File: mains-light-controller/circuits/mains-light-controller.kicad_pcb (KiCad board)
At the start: 2 copper layers, 90.5 x 83 mm, 18 parts, among them J1 Screw_Terminal_01x03, J2 Screw_Terminal_01x02, Q1 BT136-500, U1 LTV-817, U2 HLK-PM05, U3 MOC3021M, U4 WeMos_mini

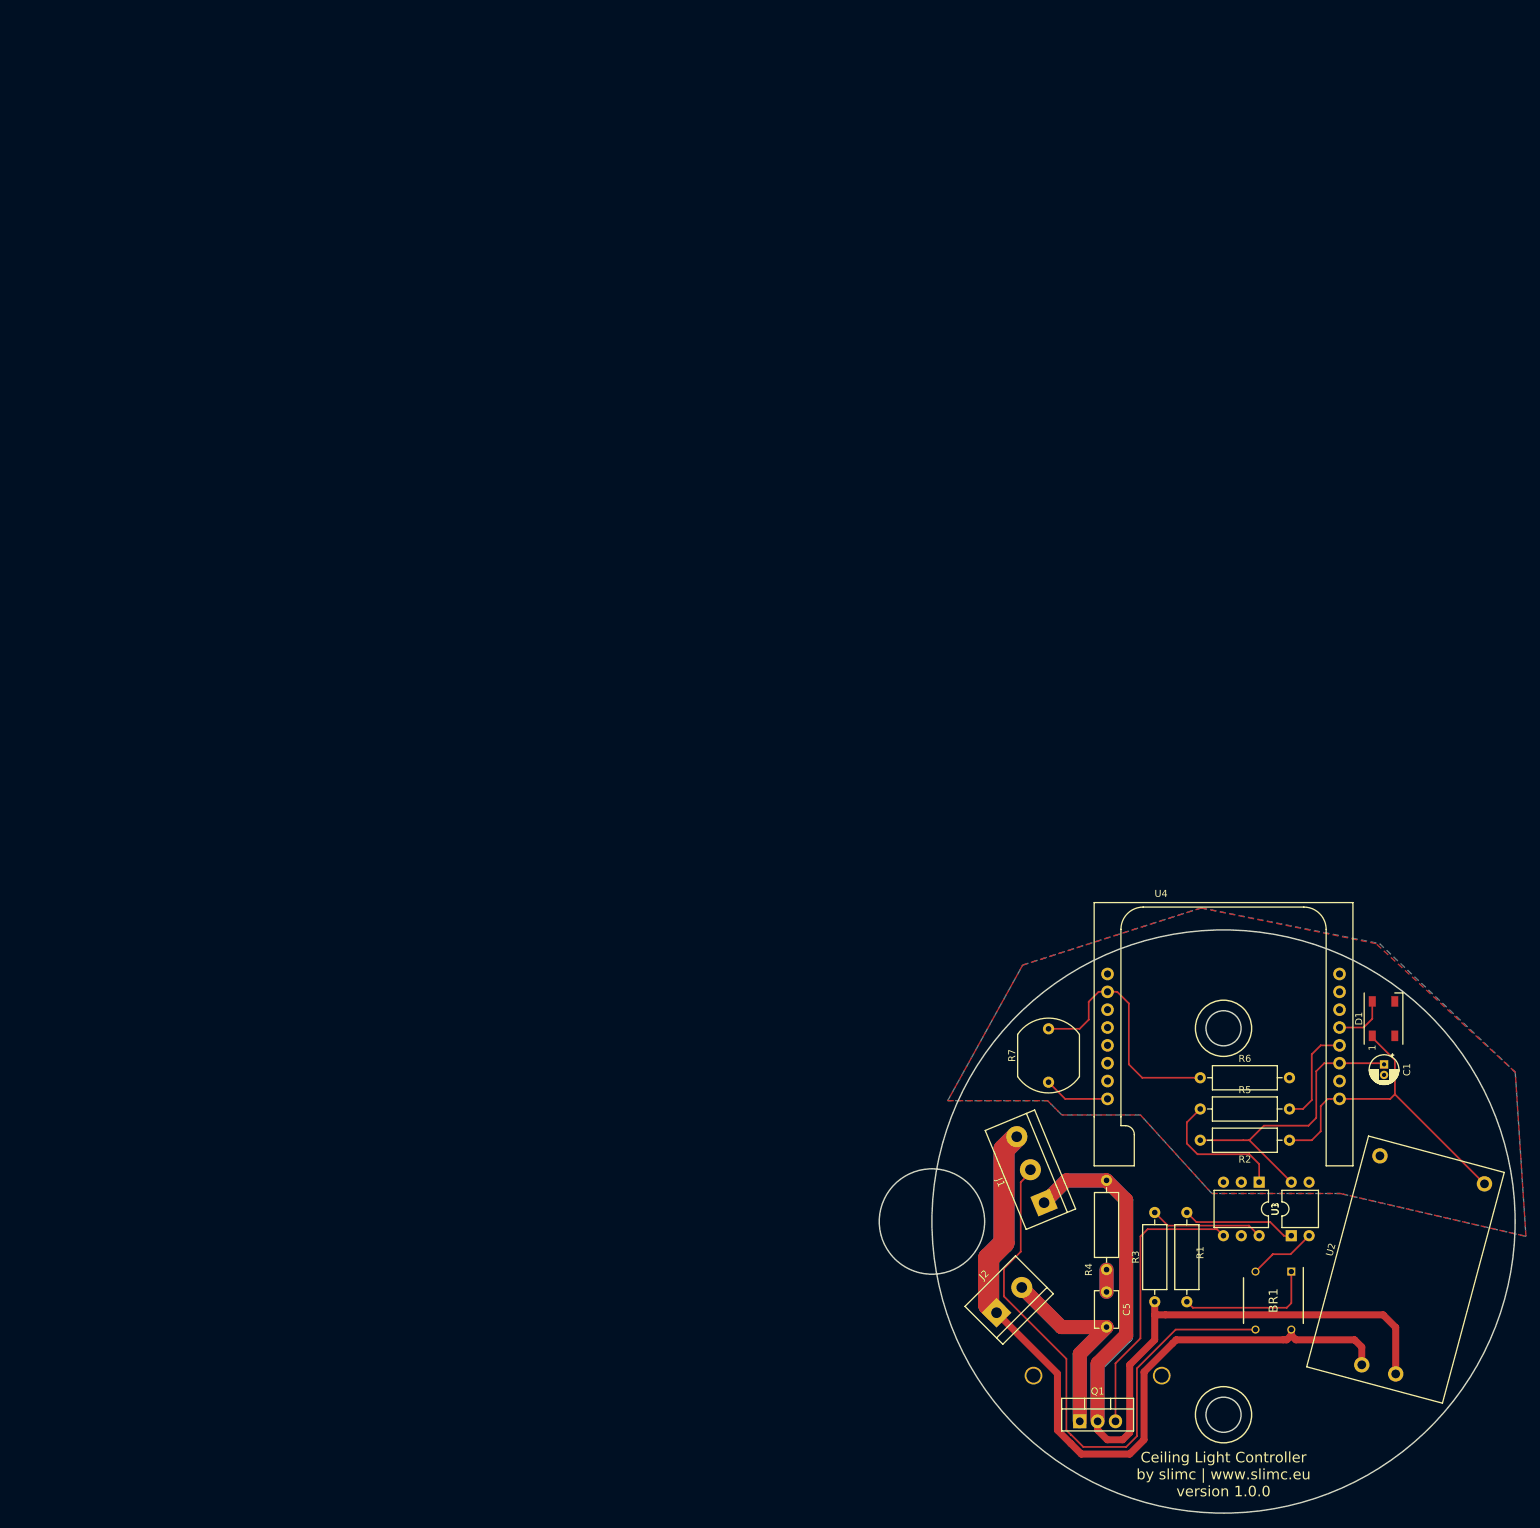
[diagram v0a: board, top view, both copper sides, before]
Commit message: improved schematic layout view; missing new PCB layout
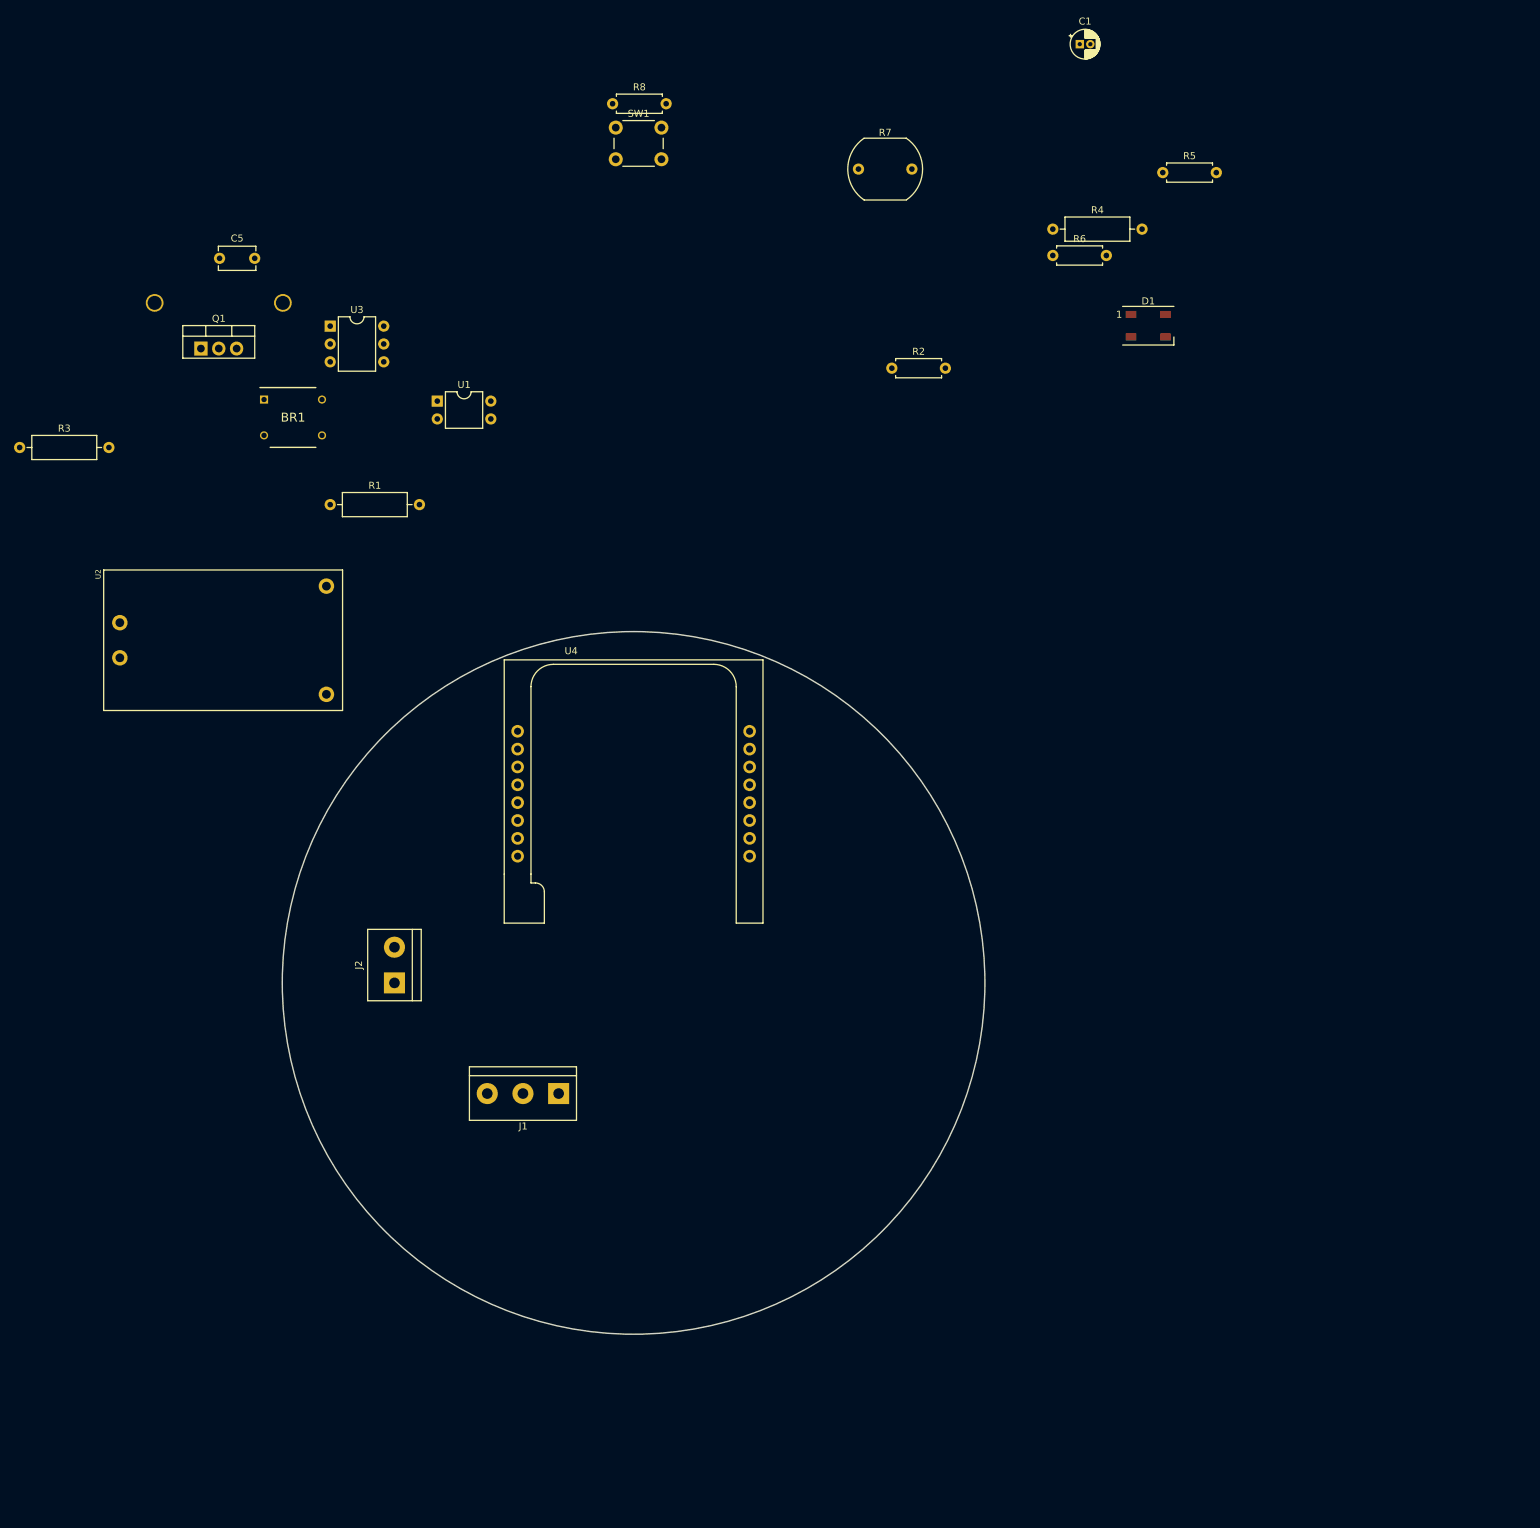
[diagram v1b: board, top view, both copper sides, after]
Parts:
- added R8: 10K, Resistor_THT:R_Axial_DIN0207_L6.3mm_D2.5mm_P7.62mm_Horizontal, F.Cu at (63.1, -59.1)
- added SW1: SW_Push, Button_Switch_THT:SW_PUSH_6mm, F.Cu at (63.5, -55.7)
- C1: value 1µf -> 1µF
- C5: value 100nf -> 100NF
- R1: value 390k -> 390K
- R2: value 10k -> 10K; footprint Resistor_THT:R_Axial_DIN0309_L9.0mm_D3.2mm_P12.70mm_Horizontal -> Resistor_THT:R_Axial_DIN0207_L6.3mm_D2.5mm_P7.62mm_Horizontal
- R3: value 10k -> 10K
- R4: value 100 -> 100R
- R5: value 330 -> 33R; footprint Resistor_THT:R_Axial_DIN0309_L9.0mm_D3.2mm_P12.70mm_Horizontal -> Resistor_THT:R_Axial_DIN0207_L6.3mm_D2.5mm_P7.62mm_Horizontal
- R6: value 10000 -> 10K; footprint Resistor_THT:R_Axial_DIN0309_L9.0mm_D3.2mm_P12.70mm_Horizontal -> Resistor_THT:R_Axial_DIN0207_L6.3mm_D2.5mm_P7.62mm_Horizontal
- U2: footprint Power_Supply:HLK-PM05 -> Power_Supply:HLK-PM01
- moved R3 202.2 mm to (-21.3, -10.2), turned to 0 degrees
- moved Q1 197.4 mm to (4.46, -24.2)
- moved C5 193.8 mm to (7.11, -37.1), turned to 0 degrees
- moved U2 190.6 mm to (7.62, 17.3), turned to 0 degrees
- moved BR1 187.8 mm to (17.6, -14.4), turned to 0 degrees
- moved U3 179.8 mm to (22.9, -27.4), turned to 0 degrees
- moved U1 169.9 mm to (38.1, -16.8), turned to 0 degrees
- moved R1 158.2 mm to (22.9, -2.03), turned to 0 degrees
- moved C1 151.5 mm to (129.5, -67.6), turned to 0 degrees
- moved R4 135.6 mm to (125.7, -41.2), turned to 0 degrees
- moved R5 133.4 mm to (141.4, -49.3)
- moved R7 132.7 mm to (98.0, -49.8), turned to 0 degrees
- moved R2 123.6 mm to (102.8, -21.4), turned to 0 degrees
- moved R6 118.9 mm to (125.7, -37.5)
- moved D1 104.1 mm to (139.3, -27.5), turned to 0 degrees
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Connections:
- net Net-(C5-Pad2) renamed L_OUT
- net Net-(R6-Pad1) renamed A0
- net Net-(U4-Pad12) renamed D5
- net Net-(U4-Pad13) renamed D6
- net Net-(U4-Pad14) renamed D7
- net Net-(U4-Pad7) renamed RX
- net Net-(U4-Pad8) renamed TX
- net Net-(U4-Pad9) renamed RST
- BR1 pad 3: Net-(BR1-Pad3) -> N_MAIN
- BR1 pad 4: Net-(BR1-Pad4) -> M1_IN
- C1 pad 1: Net-(C1-Pad1) -> D0
- D1 pad 1: Net-(D1-Pad1) -> +3V3
- D1 pad 4: Net-(D1-Pad4) -> D8
- J1 pad 1: Net-(J1-Pad1) -> N_MAIN
- J1 pad 2: Net-(BR1-Pad3) -> M2_IN
- J1 pad 3: Net-(BR1-Pad4) -> M1_IN
- J2 pad 1: Net-(BR1-Pad4) -> N_MAIN
- Q1 pad 2: Net-(J1-Pad1) -> M2_IN
- R2 pad 1: Net-(D1-Pad1) -> D0
- R2 pad 2: Net-(C1-Pad1) -> +5V
- R3 pad 1: Net-(J1-Pad1) -> M2_IN
- R4 pad 1: Net-(J1-Pad1) -> M2_IN
- R5 pad 2: Net-(R5-Pad2) -> D1
- R7 pad 1: Net-(R7-Pad1) -> +3V3
- U1 pad 4: Net-(C1-Pad1) -> D0
- U2 pad 1: Net-(BR1-Pad4) -> M2_IN
- U2 pad 2: Net-(J1-Pad1) -> N_MAIN
- U2 pad 4: Net-(D1-Pad1) -> +5V
- U4 pad 1: Net-(D1-Pad1) -> +5V
- U4 pad 11: Net-(U4-Pad11) -> D0
- U4 pad 15: Net-(U4-Pad15) -> D8
- U4 pad 16: Net-(R7-Pad1) -> +3V3
- U4 pad 3: Net-(C1-Pad1) -> D4
- U4 pad 4: Net-(R5-Pad2) -> D3
- U4 pad 5: Net-(D1-Pad4) -> D2
- U4 pad 6: Net-(U4-Pad6) -> D1
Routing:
- net Net-(J1-Pad1): track 163.5 -> 0.00 mm
- net Net-(BR1-Pad4): track 138.6 -> 0.00 mm
- net Net-(BR1-Pad3): track 82.6 -> 0.00 mm
- net L_OUT: track 58.8 -> 0.00 mm
- net Net-(D1-Pad1): track 47.5 -> 0.00 mm
- net Net-(C1-Pad1): track 43.1 -> 0.00 mm
- net Net-(Q1-Pad3): track 40.4 -> 0.00 mm
- net A0: track 35.4 -> 0.00 mm
- net Net-(BR1-Pad1): track 20.0 -> 0.00 mm
- net Net-(R5-Pad1): track 19.8 -> 0.00 mm
- net Net-(R3-Pad2): track 16.2 -> 0.00 mm
- net Net-(R1-Pad1): track 16.2 -> 0.00 mm
- net Net-(R5-Pad2): track 14.7 -> 0.00 mm
- net Net-(BR1-Pad2): track 9.77 -> 0.00 mm
- net Net-(R7-Pad1): track 9.38 -> 0.00 mm
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- removed copper zone on B.Cu, net GND
- removed copper zone on F.Cu, net GND
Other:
- board size 90.5 x 83 mm -> 100 x 100 mm
- board text removed: "Ceiling Light Controller by slimc | www.slimc.eu version 1.0.0"

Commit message: Schematic changes; PCB component placement, no traces
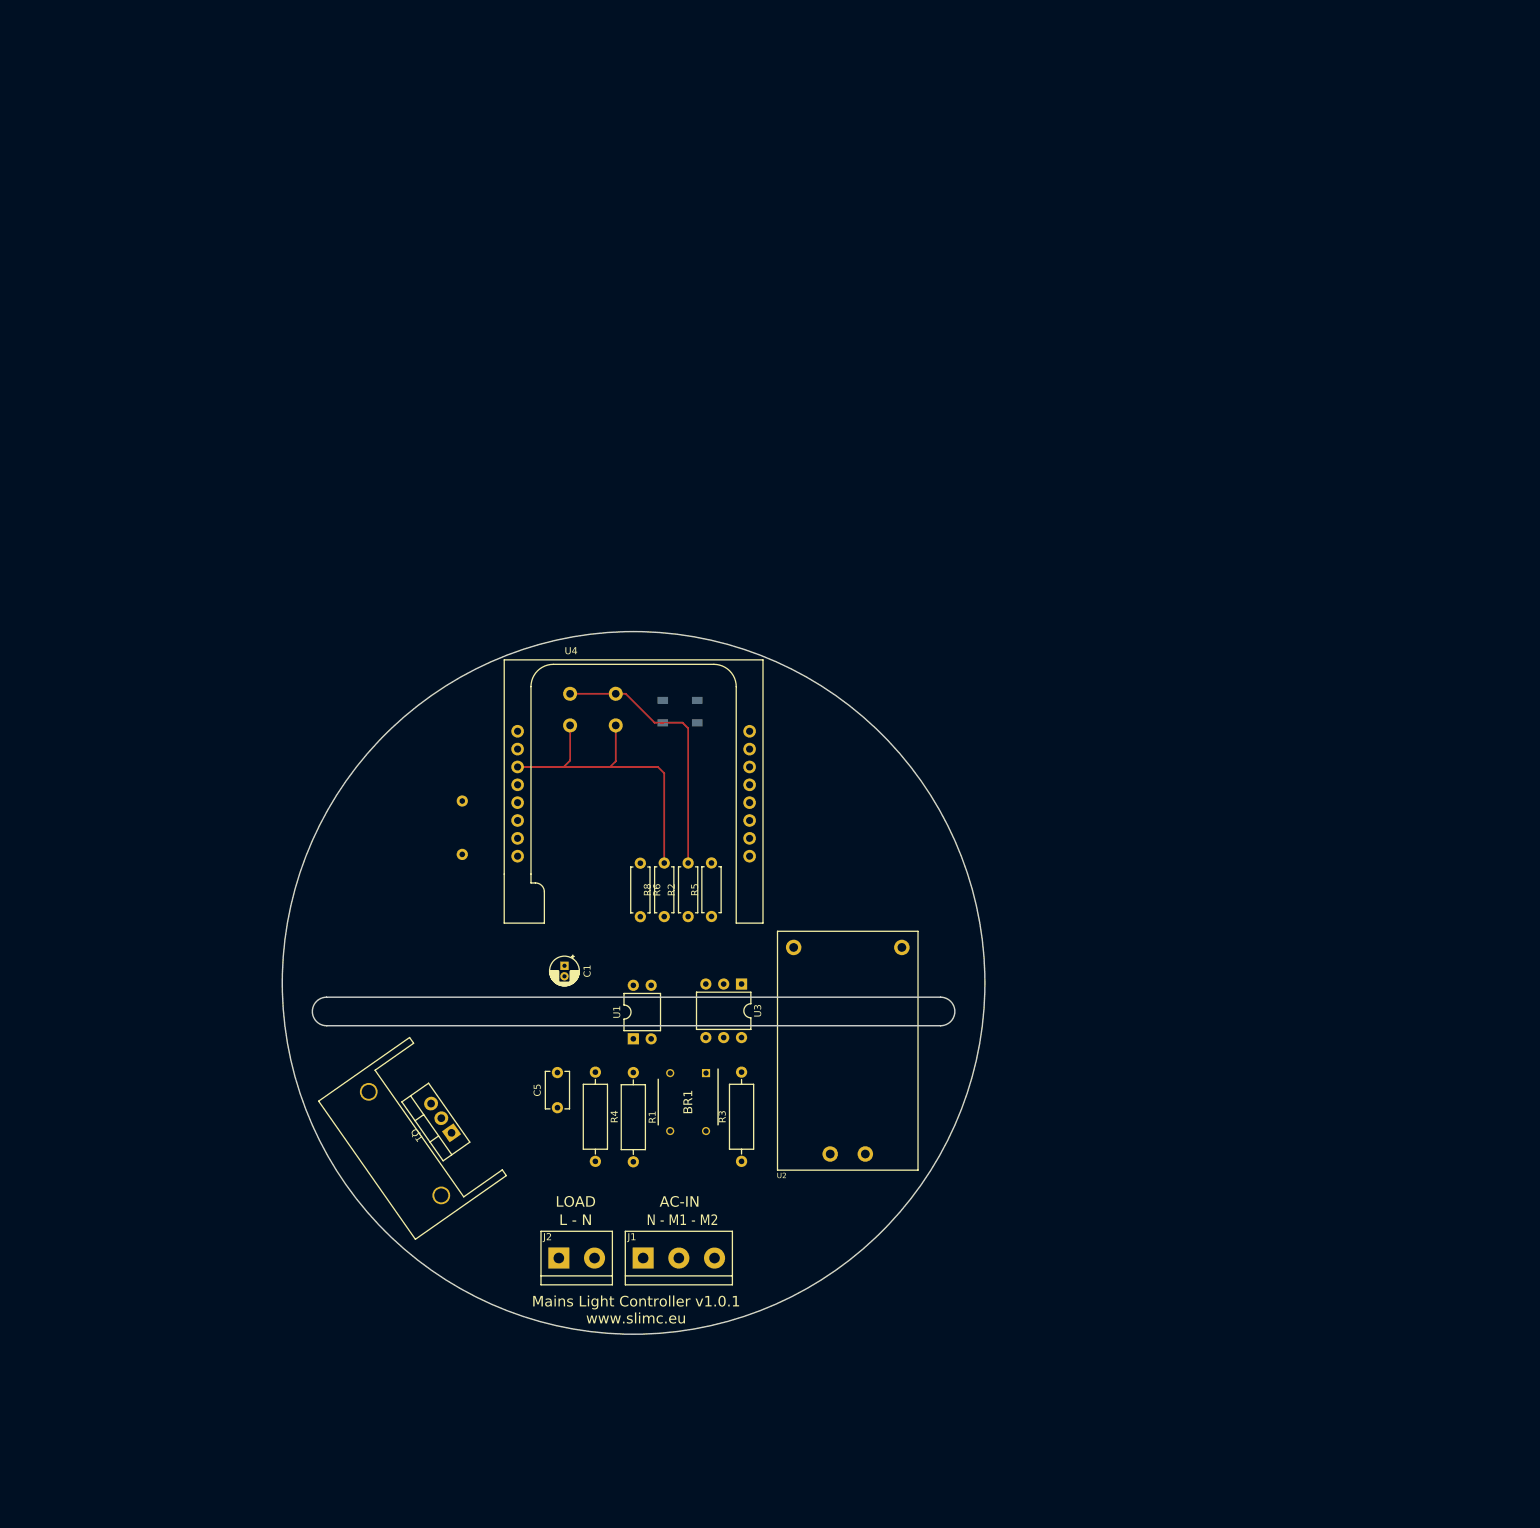
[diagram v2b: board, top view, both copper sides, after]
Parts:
- D1, R7, SW1: moved to B.Cu
- moved C1 150.3 mm to (56.2, 63.6), turned to 270 degrees
- moved R3 144.5 mm to (81.4, 91.4), turned to 90 degrees
- moved R4 136.5 mm to (60.6, 78.7), turned to 270 degrees
- moved C5 130.1 mm to (55.2, 83.8), turned to 90 degrees
- moved R5 123.8 mm to (77.1, 56.6), turned to 90 degrees
- moved Q1 117.2 mm to (40.1, 87.4), turned to 125 degrees
- moved R8 115.9 mm to (70.4, 56.6), turned to 90 degrees
- moved R7 112.7 mm to (41.7, 47.8), turned to 90 degrees
- moved BR1 112.5 mm to (73.8, 83.0), turned to 270 degrees
- moved U3 110.4 mm to (81.4, 66.2), turned to 270 degrees
- moved U2 106.4 mm to (96.5, 75.7), turned to 90 degrees
- moved R6 104.5 mm to (67.0, 49.0), turned to 270 degrees
- moved U1 95.0 mm to (66.0, 74.0), turned to 90 degrees
- moved R1 91.6 mm to (66.0, 78.8), turned to 270 degrees
- moved D1 86.4 mm to (72.6, 27.4)
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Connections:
- C1 pad 1: D0 -> D8
- D1 pad 4: D8 -> D1
- J1 pad 2: M2_IN -> M1_IN
- J1 pad 3: M1_IN -> M2_IN
- J2 pad 1: N_MAIN -> L_OUT
- J2 pad 2: L_OUT -> N_MAIN
- R2 pad 1: D0 -> D8
- R2 pad 2: +5V -> +3V3
- R5 pad 2: D1 -> D3
- R8 pad 2: D3 -> D0
- SW1 pad 1: +5V -> +3V3
- SW1 pad 2: D3 -> D0
- U1 pad 4: D0 -> D8
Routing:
- net D0: track 0.00 -> 46.6 mm
- net +3V3: track 0.00 -> 38.2 mm
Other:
- outline, holes or cut-outs redrawn
- board text added: "AC-IN"
- board text added: "L - N"
- board text added: "LOAD"
- board text added: "Mains Light Controller v1.0.1 www.slimc.eu"
- board text added: "N - M1 - M2"
